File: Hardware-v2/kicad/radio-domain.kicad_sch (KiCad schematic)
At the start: 29 parts, among them J2 RF/COAXIAL SMA BHD JACK STR 5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, U7 W25Q16JW, U8 Si4684-A10-GM, Y2 ABM8-19.200MHZ-10-1-U-T

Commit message: Correct the v2 EEPROM footprint and crystal load capacitors
Compared the ADAU1452 section with the EVAL-ADAU1452REVBZ user guide
(UG-1662) and the ADAU1452 datasheet.

- U14: 25AA1024-I/SM is a 208 mil SOIJ-8, but it was on a 150 mil SOIC
  footprint. Use Package_SO:SOIC-8_5.3x5.3mm_P1.27mm and fix the PNM.
- C141/C142 (Y3): 15 pF NP0 instead of 12 pF X7R.
- C139/C140 (Y2): 12 pF NP0 instead of 12 pF X7R.
- C6: add 1 uF on 1V2 near U13 pin 20, which the datasheet asks for.
- Widen the 1V2 trace from U13 pin 20 to 0.35 mm.

Co-Authored-By: Claude Opus 5.5 (1M context) <noreply@anthropic.com>
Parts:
- C139, C140: PNM C0603C120K5RACTU -> CC0603JRNPO9BN120
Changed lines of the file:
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@@
 			)
 		)
-		(property "Description" "12pF X7R ±10% 50V 0603 Ceramic Capacitors RoHS"
+		(property "Description" "CAP CER 12pF 50V NP0 0603"
 			(at 138.43 68.58 0)
 			(hide yes)
@@
 			)
 		)
-		(property "PNM" "C0603C120K5RACTU"
+		(property "PNM" "CC0603JRNPO9BN120"
 			(at 138.43 68.58 90)
 			(hide yes)
@@
 			)
 		)
-		(property "Description" "12pF X7R ±10% 50V 0603 Ceramic Capacitors RoHS"
+		(property "Description" "CAP CER 12pF 50V NP0 0603"
 			(at 138.43 86.36 0)
 			(hide yes)
@@
 			)
 		)
-		(property "PNM" "C0603C120K5RACTU"
+		(property "PNM" "CC0603JRNPO9BN120"
 			(at 138.43 86.36 90)
 			(hide yes)

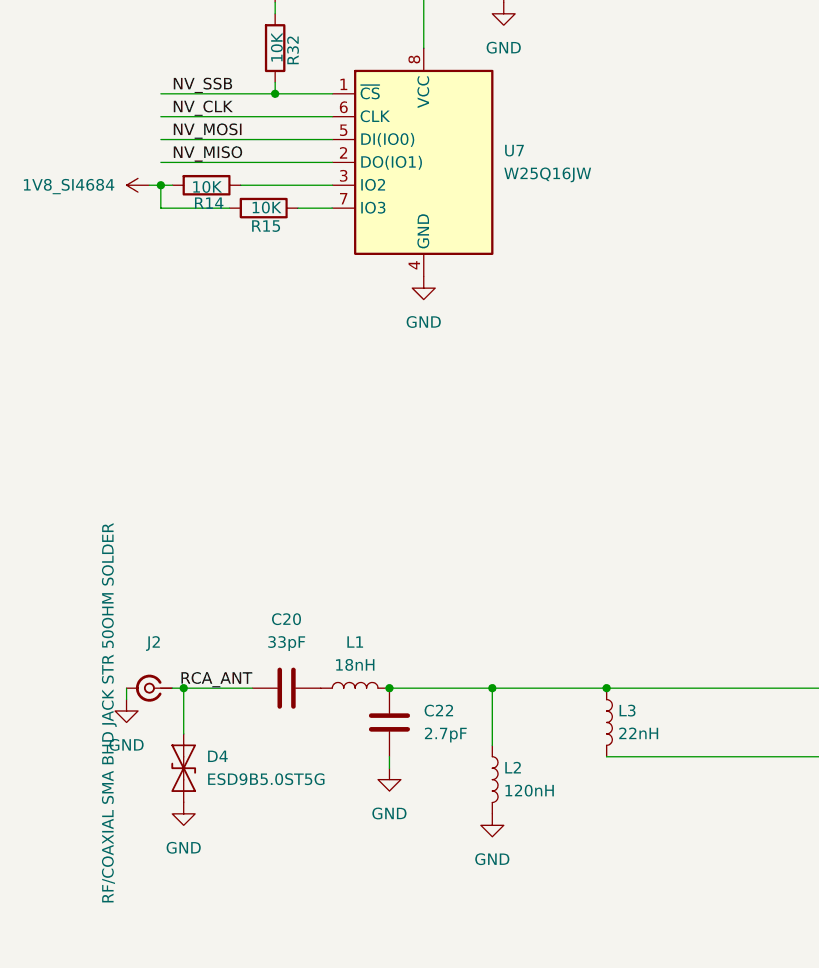
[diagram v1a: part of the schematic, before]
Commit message: Add the TOSLINK output to the v2 board
Fit an Everlight PLT237/T10WH as J5 on the top edge, driven from
ADAU1452 SPDIFOUT through R56, with FB3 and C65 on its 3V3_AUDIO
supply. The optical face sits 2.31 mm past the board edge.

Move flash U3 and its parts next to U8 and U13 to free the edge, which
shortens the M_SPI traces from 80-95 mm to 34-46 mm.

Pin order follows the LCSC footprint: pad 1 Vin, 2 Vcc, 3 GND.

Co-Authored-By: Claude <noreply@anthropic.com>
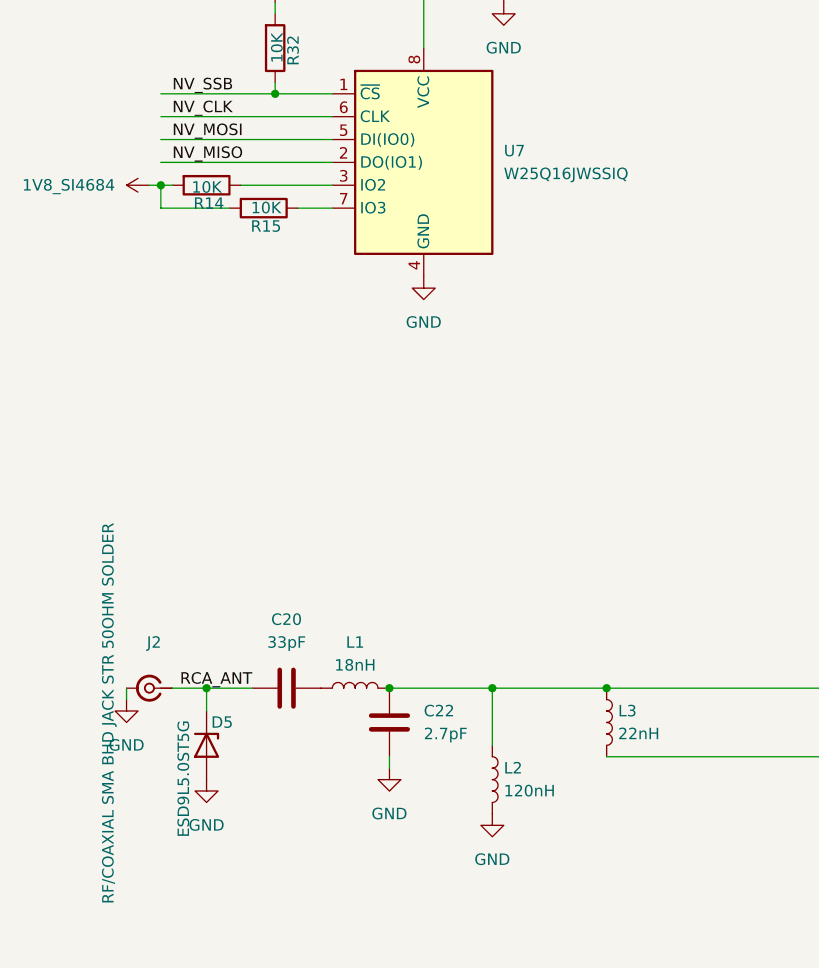
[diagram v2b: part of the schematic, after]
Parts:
- removed D4: ESD9B5.0ST5G, Diode_SMD:D_SOD-923, symbol Diode:ESD9B5.0ST5G
- added D5: ESD9L5.0ST5G, Diode_SMD:D_SOD-923, symbol Device:D_Zener
- U7: value W25Q16JW -> W25Q16JWSSIQ; PNM W25Q16JW -> W25Q16JWSSIQ
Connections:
- net GND: now also D5.2 (A)
- net RCA_ANT: now also D5.1 (K)
